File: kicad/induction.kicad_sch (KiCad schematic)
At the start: 40 parts, among them Q1 PMOS, Q10 NJFET, Q2 NMOS, Q3 NMOS, Q4 NMOS, Q5 NMOS, Q6 NPN, Q7 NMOS, Q8 PMOS, Q9 NPN, T1 Transformer_1P_1S, T2 Transformer_1P_1S, Y1 Crystal

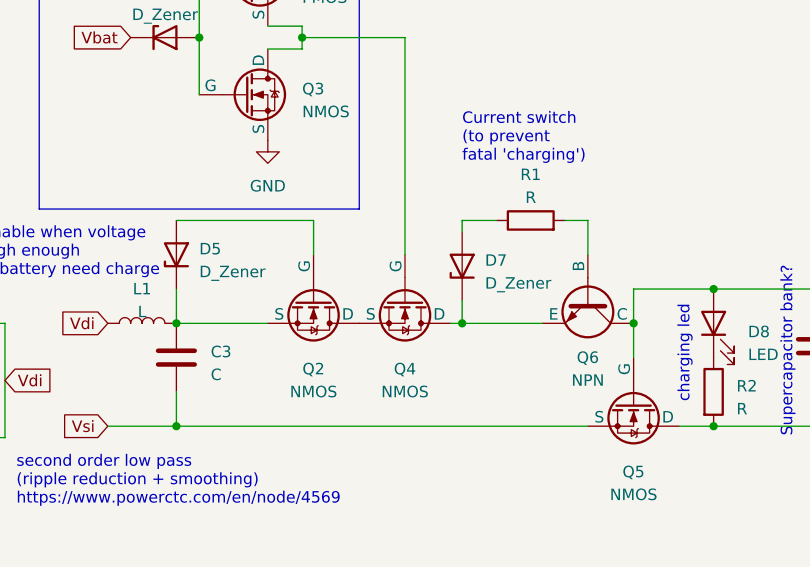
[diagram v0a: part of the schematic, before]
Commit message: Fix transistors on charge management
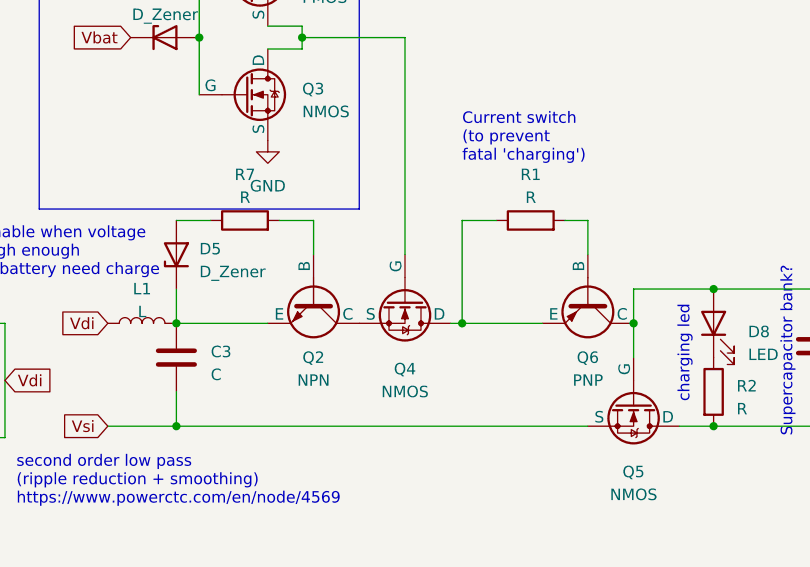
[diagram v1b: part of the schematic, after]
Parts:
- removed D7: D_Zener, symbol Device:D_Zener
- removed Q2: NMOS, symbol Simulation_SPICE:NMOS
- removed Q6: NPN, symbol Simulation_SPICE:NPN
- added Q2: NPN, symbol Simulation_SPICE:NPN
- added Q6: PNP, symbol Simulation_SPICE:PNP
- added R7: R, symbol Device:R
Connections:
- net Vbat: now also Q6.1 (C)
- net at R1.2: now also Q6.2 (B)
- net at Q4.1 (D): now also R1.1, Q6.3 (E)
- net at C3.1, D5.1 (K), L1.2: now also Q2.3 (E)
- net at D5.2 (A): now also R7.1
- net at Q4.3 (S): now also Q2.1 (C)
- new net: Q2.2 (B), R7.2
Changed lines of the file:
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@@
-    (stroke (width 0) (type default))
-  )
-  (wire (pts (xy 182.88 73.66) (xy 198.12 73.66))
     (stroke (width 0) (type default))
   )
@@
     (stroke (width 0) (type default))
   )
+  (wire (pts (xy 182.88 73.66) (xy 186.69 73.66))
+    (stroke (width 0) (type default))
+  )
+  (wire (pts (xy 194.31 73.66) (xy 198.12 73.66))
+    (stroke (width 0) (type default))
+  )
   (wire (pts (xy 148.59 97.79) (xy 144.78 97.79))
     (stroke (width 0) (type default))
   )
-  (wire (pts (xy 214.63 74.93) (xy 214.63 73.66))
-    (stroke (width 0) (type default))
-  )
   (wire (pts (xy 156.21 97.79) (xy 163.83 97.79))
     (stroke (width 0) (type default))
@@
     (stroke (width 0) (type default))
   )
-  (wire (pts (xy 233.68 85.09) (xy 233.68 81.28))
+  (wire (pts (xy 233.68 81.28) (xy 233.68 85.09))
     (stroke (width 0) (type default))
   )
@@
     (stroke (width 0) (type default))
   )
-  (wire (pts (xy 214.63 85.09) (xy 214.63 82.55))
-    (stroke (width 0) (type default))
-  )
   (wire (pts (xy 233.68 85.09) (xy 233.68 88.9))
+    (stroke (width 0) (type default))
+  )
+  (wire (pts (xy 214.63 73.66) (xy 214.63 85.09))
     (stroke (width 0) (type default))
   )
@@
     )
   )
-  (symbol (lib_id "Simulation_SPICE:NPN") (at 228.6 82.55 270) (unit 1)
-    (in_bom yes) (on_board yes) (dnp no) (fields_autoplaced)
-    (property "Reference" "Q6" (at 228.6 88.9 90)
-      (effects (font (size 1.27 1.27)))
-    )
-    (property "Value" "NPN" (at 228.6 91.44 90)
-      (effects (font (size 1.27 1.27)))
-    )
-    (property "Footprint" "" (at 228.6 146.05 0)
-      (effects (font (size 1.27 1.27)) hide)
-    )
-    (property "Datasheet" "~" (at 228.6 146.05 0)
-      (effects (font (size 1.27 1.27)) hide)
-    )
-    (property "Sim.Device" "NPN" (at 228.6 82.55 0)
-      (effects (font (size 1.27 1.27)) hide)
-    )
-    (property "Sim.Type" "GUMMELPOON" (at 228.6 82.55 0)
-      (effects (font (size 1.27 1.27)) hide)
-    )
-    (property "Sim.Pins" "1=C 2=B 3=E" (at 228.6 82.55 0)
-      (effects (font (size 1.27 1.27)) hide)
-    )
-    (pin "1")
-    (pin "2")
-    (pin "3")
-    (instances
-      (project "kicad"
-        (path "/85f8f747-8376-4af6-9da4-afbb0f4bcd36/c5aef724-8676-4c81-889e-041c5ca81271"
-          (reference "Q6") (unit 1)
-        )
-      )
-    )
-  )
   (symbol (lib_id "Device:D") (at 152.4 97.79 180) (unit 1)
     (in_bom yes) (on_board yes) (dnp no) (fields_autoplaced)
@@
     )
   )
-  (symbol (lib_id "Simulation_SPICE:NMOS") (at 198.12 82.55 270) (unit 1)
-    (in_bom yes) (on_board yes) (dnp no) (fields_autoplaced)
-    (property "Reference" "Q2" (at 198.12 90.17 90)
-      (effects (font (size 1.27 1.27)))
-    )
-    (property "Value" "NMOS" (at 198.12 92.71 90)
-      (effects (font (size 1.27 1.27)))
-    )
-    (property "Footprint" "" (at 200.66 87.63 0)
-      (effects (font (size 1.27 1.27)) hide)
-    )
-    (property "Datasheet" "https://ngspice.sourceforge.io/docs/ngspice-manual.pdf" (at 185.42 82.55 0)
-      (effects (font (size 1.27 1.27)) hide)
-    )
-    (property "Sim.Device" "NMOS" (at 180.975 82.55 0)
-      (effects (font (size 1.27 1.27)) hide)
-    )
-    (property "Sim.Type" "VDMOS" (at 179.07 82.55 0)
-      (effects (font (size 1.27 1.27)) hide)
-    )
-    (property "Sim.Pins" "1=D 2=G 3=S" (at 182.88 82.55 0)
+  (symbol (lib_id "Device:R") (at 29.21 78.74 0) (unit 1)
+    (in_bom yes) (on_board yes) (dnp no) (fields_autoplaced)
+    (property "Reference" "R3" (at 31.75 78.105 0)
+      (effects (font (size 1.27 1.27)) (justify left))
+    )
+    (property "Value" "R" (at 31.75 80.645 0)
+      (effects (font (size 1.27 1.27)) (justify left))
+    )
+    (property "Footprint" "" (at 27.432 78.74 90)
+      (effects (font (size 1.27 1.27)) hide)
+    )
+    (property "Datasheet" "~" (at 29.21 78.74 0)
+      (effects (font (size 1.27 1.27)) hide)
+    )
+    (pin "1")
+    (pin "2")
+    (instances
+      (project "kicad"
+        (path "/85f8f747-8376-4af6-9da4-afbb0f4bcd36/c5aef724-8676-4c81-889e-041c5ca81271"
+          (reference "R3") (unit 1)
+        )
+      )
+    )
+  )
+  (symbol (lib_id "Simulation_SPICE:NPN") (at 198.12 82.55 270) (unit 1)
+    (in_bom yes) (on_board yes) (dnp no) (fields_autoplaced)
+    (property "Reference" "Q2" (at 198.12 88.9 90)
+      (effects (font (size 1.27 1.27)))
+    )
+    (property "Value" "NPN" (at 198.12 91.44 90)
+      (effects (font (size 1.27 1.27)))
+    )
+    (property "Footprint" "" (at 198.12 146.05 0)
+      (effects (font (size 1.27 1.27)) hide)
+    )
+    (property "Datasheet" "~" (at 198.12 146.05 0)
+      (effects (font (size 1.27 1.27)) hide)
+    )
+    (property "Sim.Device" "NPN" (at 198.12 82.55 0)
+      (effects (font (size 1.27 1.27)) hide)
+    )
+    (property "Sim.Type" "GUMMELPOON" (at 198.12 82.55 0)
+      (effects (font (size 1.27 1.27)) hide)
+    )
+    (property "Sim.Pins" "1=C 2=B 3=E" (at 198.12 82.55 0)
       (effects (font (size 1.27 1.27)) hide)
     )
@@
         (path "/85f8f747-8376-4af6-9da4-afbb0f4bcd36/c5aef724-8676-4c81-889e-041c5ca81271"
           (reference "Q2") (unit 1)
-        )
-      )
-    )
-  )
-  (symbol (lib_id "Device:R") (at 29.21 78.74 0) (unit 1)
-    (in_bom yes) (on_board yes) (dnp no) (fields_autoplaced)
-    (property "Reference" "R3" (at 31.75 78.105 0)
-      (effects (font (size 1.27 1.27)) (justify left))
-    )
-    (property "Value" "R" (at 31.75 80.645 0)
-      (effects (font (size 1.27 1.27)) (justify left))
-    )
-    (property "Footprint" "" (at 27.432 78.74 90)
-      (effects (font (size 1.27 1.27)) hide)
-    )
-    (property "Datasheet" "~" (at 29.21 78.74 0)
-      (effects (font (size 1.27 1.27)) hide)
-    )
-    (pin "1")
-    (pin "2")
-    (instances
-      (project "kicad"
-        (path "/85f8f747-8376-4af6-9da4-afbb0f4bcd36/c5aef724-8676-4c81-889e-041c5ca81271"
-          (reference "R3") (unit 1)
         )
       )
@@
     )
   )
-  (symbol (lib_id "Device:D_Zener") (at 214.63 78.74 90) (unit 1)
-    (in_bom yes) (on_board yes) (dnp no) (fields_autoplaced)
-    (property "Reference" "D7" (at 217.17 78.105 90)
-      (effects (font (size 1.27 1.27)) (justify right))
-    )
-    (property "Value" "D_Zener" (at 217.17 80.645 90)
-      (effects (font (size 1.27 1.27)) (justify right))
-    )
-    (property "Footprint" "" (at 214.63 78.74 0)
-      (effects (font (size 1.27 1.27)) hide)
-    )
-    (property "Datasheet" "~" (at 214.63 78.74 0)
-      (effects (font (size 1.27 1.27)) hide)
-    )
-    (pin "1")
-    (pin "2")
-    (instances
-      (project "kicad"
-        (path "/85f8f747-8376-4af6-9da4-afbb0f4bcd36/c5aef724-8676-4c81-889e-041c5ca81271"
-          (reference "D7") (unit 1)
-        )
-      )
-    )
-  )
   (symbol (lib_id "Simulation_SPICE:NMOS") (at 208.28 82.55 270) (unit 1)
     (in_bom yes) (on_board yes) (dnp no) (fields_autoplaced)
@@
         )
       )
+    )
+  )
+  (symbol (lib_id "Simulation_SPICE:PNP") (at 228.6 82.55 270) (unit 1)
+    (in_bom yes) (on_board yes) (dnp no) (fields_autoplaced)
+    (property "Reference" "Q6" (at 228.6 88.9 90)
+      (effects (font (size 1.27 1.27)))
+    )
+    (property "Value" "PNP" (at 228.6 91.44 90)
+      (effects (font (size 1.27 1.27)))
+    )
+    (property "Footprint" "" (at 228.6 118.11 0)
+      (effects (font (size 1.27 1.27)) hide)
+    )
+    (property "Datasheet" "~" (at 228.6 118.11 0)
+      (effects (font (size 1.27 1.27)) hide)
+    )
+    (property "Sim.Device" "PNP" (at 228.6 82.55 0)
+      (effects (font (size 1.27 1.27)) hide)
+    )
+    (property "Sim.Type" "GUMMELPOON" (at 228.6 82.55 0)
+      (effects (font (size 1.27 1.27)) hide)
+    )
+    (property "Sim.Pins" "1=C 2=B 3=E" (at 228.6 82.55 0)
+      (effects (font (size 1.27 1.27)) hide)
+    )
+    (pin "1")
+    (pin "2")
+    (pin "3")
+    (instances
+      (project "kicad"
+        (path "/85f8f747-8376-4af6-9da4-afbb0f4bcd36/c5aef724-8676-4c81-889e-041c5ca81271"
+          (reference "Q6") (unit 1)
+        )
+      )
+    )
+  )
+  (symbol (lib_id "Device:R") (at 190.5 73.66 90) (unit 1)
+    (in_bom yes) (on_board yes) (dnp no) (fields_autoplaced)
+    (property "Reference" "R7" (at 190.5 68.58 90)
+      (effects (font (size 1.27 1.27)))
+    )
+    (property "Value" "R" (at 190.5 71.12 90)
+      (effects (font (size 1.27 1.27)))
+    )
+    (property "Footprint" "" (at 190.5 75.438 90)
+      (effects (font (size 1.27 1.27)) hide)
+    )
+    (property "Datasheet" "~" (at 190.5 73.66 0)
+      (effects (font (size 1.27 1.27)) hide)
+    )
+    (pin "1")
+    (pin "2")
+    (instances
+      (project "kicad"
+        (path "/85f8f747-8376-4af6-9da4-afbb0f4bcd36/c5aef724-8676-4c81-889e-041c5ca81271"
+          (reference "R7") (unit 1)
+        )
+      )

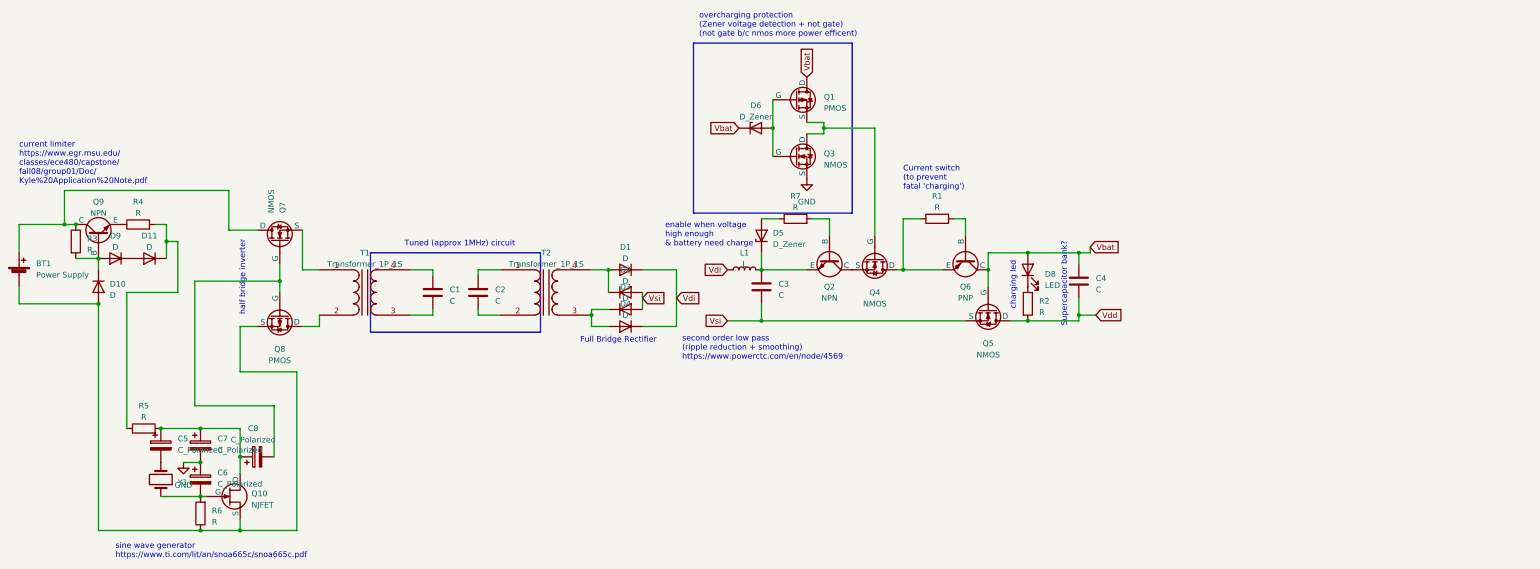
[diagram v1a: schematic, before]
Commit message: Add pulldown resistors
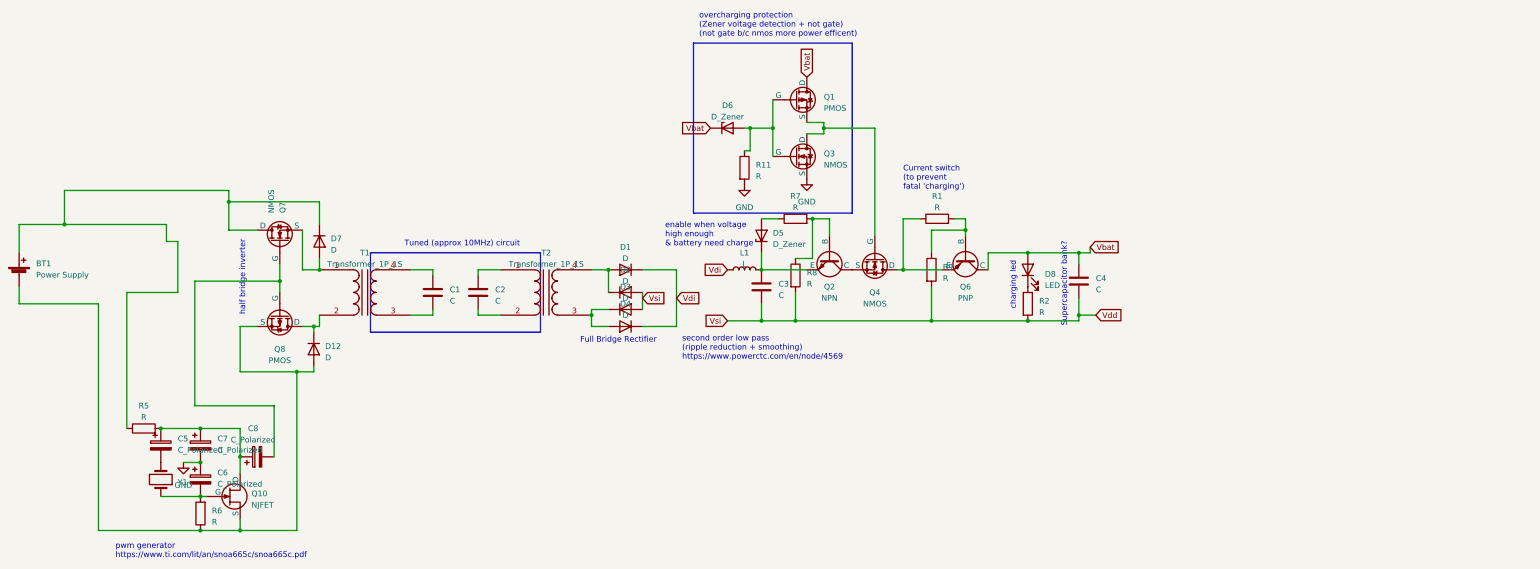
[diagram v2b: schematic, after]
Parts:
- removed D10, D11, D9: D, symbol Device:D
- removed Q5: NMOS, symbol Simulation_SPICE:NMOS
- removed Q9: NPN, symbol Simulation_SPICE:NPN
- removed R3, R4: R, symbol Device:R
- added D12, D7: D, symbol Device:D
- added R11, R8, R9: R, symbol Device:R
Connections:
- net Vsi is gone; now on net Vdd: C3.2, D2.2 (A), D3.2 (A)
- net GND: now also R11.2
- net Vdd: now also R8.2, R9.2
- net at D6.2 (A), Q1.2 (G), Q3.2 (G): now also R11.1
- net at BT1.1 (+), Q7.1 (D): now also R5.1, D7.1 (K)
- net at Q7.3 (S), T1.1 (AA): now also D7.2 (A)
- net at BT1.2 (-), Q10.3 (S), Q8.3 (S)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: now also D12.2 (A)
- net at Q2.2 (B), R7.2: now also R8.1
- net at Q6.2 (B), R1.2: now also R9.1
- net at Q8.1 (D), T1.2 (AB): now also D12.1 (K)
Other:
- note added: "Tuned (approx 10MHz) circuit"
- note added: "pwm generator https://www.ti.com/lit/an/snoa665c/snoa665c.pdf"
- note removed: "Tuned (approx 1MHz) circuit"
- note removed: "current limiter https://www.egr.msu.edu/ classes/ece480/capstone/ fall08/group01/Doc/ Kyle%20Application%20Note.pdf"
- note removed: "sine wave generator https://www.ti.com/lit/an/snoa665c/snoa665c.pdf"
- moved on the sheet: D6

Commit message: Create subcircuit sheets
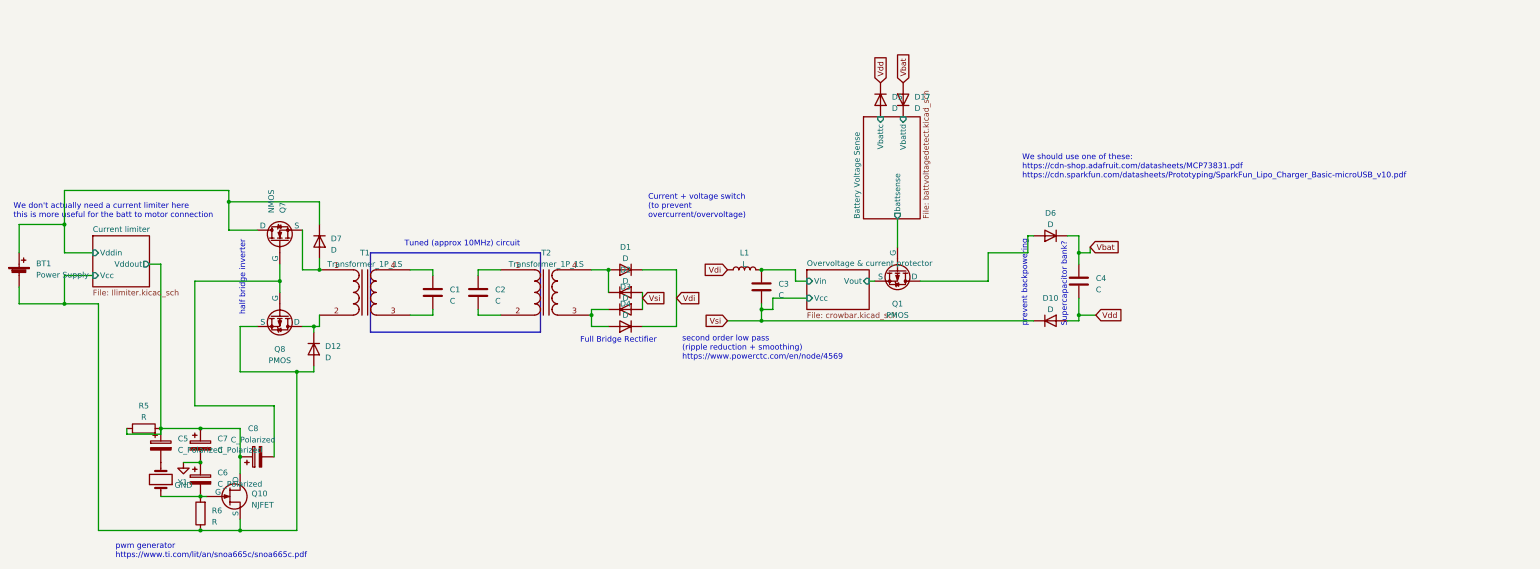
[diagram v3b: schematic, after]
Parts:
- removed D5, D6: D_Zener, symbol Device:D_Zener
- removed D8: LED, symbol Device:LED
- removed Q2: NPN, symbol Simulation_SPICE:NPN
- removed Q3, Q4: NMOS, symbol Simulation_SPICE:NMOS
- removed Q6: PNP, symbol Simulation_SPICE:PNP
- removed R1, R11, R2, R7, R8, R9: R, symbol Device:R
- added D10, D17, D5, D6: D, symbol Device:D
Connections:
- net Vbat: now also D17.2 (A), D6.1 (K); no longer Q1.1 (D)
- net Vdd: now also D10.2 (A), D5.1 (K); no longer C3.2, D2.2 (A), D3.2 (A)
- net Battery Voltage Sense/battsense: now reaches Q1.2 (G)
- net Current limiter/Vddout: now reaches C5.1, C7.1, C8.1, Q10.1 (D), R5.2
- net Current limiter/Vddout: now also R5.1
- net Current limiter/Vddin: now reaches BT1.1 (+), D7.1 (K), Q7.1 (D)
- net Current limiter/Vddin: no longer R5.1
- net Overvoltage & current protector/Vin: now reaches C3.1, L1.2
- net Overvoltage & current protector/Vout: now reaches Q1.3 (S)
- net Current limiter/Vcc: now reaches BT1.2 (-), D12.2 (A), Q10.3 (S), Q8.3 (S), R6.1
- new net: D6.2 (A), Q1.1 (D)
- new net Battery Voltage Sense/Vbattc: D5.2 (A)
- new net Battery Voltage Sense/Vbattd: D17.1 (K)
- new net Vsi: C3.2, D10.1 (K), D2.2 (A), D3.2 (A)
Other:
- added sheet Battery Voltage Sense (battvoltagedetect.kicad_sch)
- added sheet Current limiter (Ilimiter.kicad_sch)
- added sheet Overvoltage & current protector (crowbar.kicad_sch)
- note added: "Current + voltage switch (to prevent overcurrent/overvoltage)"
- note added: "We don't actually need a current limiter here this is more useful for the batt to motor connection"
- note added: "We should use one of these: https://cdn-shop.adafruit.com/datasheets/MCP73831.pdf https://cdn.sparkfun.com/datasheets/Prototyping/SparkFun_Lipo_Charger_Basic-microUSB_v10.pdf"
- note added: "prevent backpowering"
- note removed: "Current switch (to prevent fatal 'charging')"
- note removed: "charging led"
- note removed: "enable when voltage high enough & battery need charge"
- note removed: "overcharging protection (Zener voltage detection + not gate) (not gate b/c nmos more power efficent)"
